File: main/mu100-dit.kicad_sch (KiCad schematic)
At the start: 14 parts, among them J1 Conn_01x10_Female, U1 TOTX-177L, U2 AK4103A

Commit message: Add reset circuit, remove need for reset
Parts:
- added C3: 0.1u/35V, Capacitor_SMD:C_0805_2012Metric_Pad1.18x1.45mm_HandSolder, symbol Device:C_Small
- added U3: APX809S-46SR-7, Package_TO_SOT_SMD:SOT-23_Handsoldering, symbol APX809S:APX809S-46SR-7
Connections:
- net +5V: now also C3.2, U3.3 (VCC)
- net GND: now also C3.1, U3.2 (GND)
- net RESET: now also U3.1 (*RESET); no longer J1.1 (Pin_1)
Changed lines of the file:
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@@
   (junction (at 115.57 130.81) (diameter 0) (color 0 0 0 0)
   )
+  (junction (at 97.79 108.585) (diameter 0) (color 0 0 0 0)
+  )
   (junction (at 53.34 81.28) (diameter 0) (color 0 0 0 0)
+  )
+  (junction (at 59.055 108.585) (diameter 0) (color 0 0 0 0)
   )
   (junction (at 58.42 83.185) (diameter 0) (color 0 0 0 0)
@@
     (stroke (width 0) (type solid) (color 0 0 0 0))
   )
+  (wire (pts (xy 97.79 104.14) (xy 97.79 108.585))
+    (stroke (width 0) (type default) (color 0 0 0 0))
+  )
   (wire (pts (xy 213.36 87.63) (xy 209.55 87.63))
     (stroke (width 0) (type default) (color 0 0 0 0))
@@
     (stroke (width 0) (type solid) (color 0 0 0 0))
   )
+  (wire (pts (xy 98.425 108.585) (xy 97.79 108.585))
+    (stroke (width 0) (type default) (color 0 0 0 0))
+  )
   (wire (pts (xy 168.91 100.33) (xy 213.36 100.33))
     (stroke (width 0) (type default) (color 0 0 0 0))
@@
     (stroke (width 0) (type solid) (color 0 0 0 0))
   )
+  (wire (pts (xy 59.055 108.585) (xy 82.55 108.585))
+    (stroke (width 0) (type default) (color 0 0 0 0))
+  )
   (wire (pts (xy 60.325 90.805) (xy 78.105 90.805))
     (stroke (width 0) (type default) (color 0 0 0 0))
   )
+  (wire (pts (xy 98.425 121.92) (xy 98.425 108.585))
+    (stroke (width 0) (type default) (color 0 0 0 0))
+  )
   (wire (pts (xy 168.91 125.73) (xy 179.07 125.73))
     (stroke (width 0) (type solid) (color 0 0 0 0))
@@
     (stroke (width 0) (type default) (color 0 0 0 0))
   )
+  (wire (pts (xy 57.785 108.585) (xy 59.055 108.585))
+    (stroke (width 0) (type default) (color 0 0 0 0))
+  )
   (wire (pts (xy 60.96 80.645) (xy 78.105 80.645))
     (stroke (width 0) (type default) (color 0 0 0 0))
@@
     (stroke (width 0) (type default) (color 0 0 0 0))
   )
+  (wire (pts (xy 57.785 121.92) (xy 57.785 108.585))
+    (stroke (width 0) (type default) (color 0 0 0 0))
+  )
   (wire (pts (xy 200.025 94.615) (xy 209.55 94.615))
     (stroke (width 0) (type default) (color 0 0 0 0))
@@
     (stroke (width 0) (type solid) (color 0 0 0 0))
   )
+  (wire (pts (xy 97.79 108.585) (xy 87.63 108.585))
+    (stroke (width 0) (type default) (color 0 0 0 0))
+  )
   (wire (pts (xy 53.34 81.28) (xy 58.42 81.28))
     (stroke (width 0) (type default) (color 0 0 0 0))
@@
     (stroke (width 0) (type solid) (color 0 0 0 0))
   )
+  (wire (pts (xy 101.6 124.46) (xy 98.425 124.46))
+    (stroke (width 0) (type default) (color 0 0 0 0))
+  )
   (wire (pts (xy 119.38 107.95) (xy 133.35 107.95))
     (stroke (width 0) (type solid) (color 0 0 0 0))
@@
   (label "RESET" (at 179.07 125.73 180)
     (effects (font (size 1.27 1.27)) (justify right bottom))
+  )
+  (label "RESET" (at 101.6 124.46 0)
+    (effects (font (size 1.27 1.27)) (justify left bottom))
   )
   (label "MCLK" (at 119.38 105.41 0)
@@
   )
   (label "LRCK" (at 61.595 95.885 0)
-    (effects (font (size 1.27 1.27)) (justify left bottom))
-  )
-  (label "RESET" (at 60.96 73.025 0)
     (effects (font (size 1.27 1.27)) (justify left bottom))
   )
@@
     (pin "1")
   )
+  (symbol (lib_id "Device:C_Small") (at 85.09 108.585 90) (mirror x) (unit 1)
+    (in_bom yes) (on_board yes)
+    (property "Reference" "C3" (id 0) (at 85.09 102.235 90))
+    (property "Value" "0.1u/35V" (id 1) (at 85.09 104.775 90))
+    (property "Footprint" "Capacitor_SMD:C_0805_2012Metric_Pad1.18x1.45mm_HandSolder" (id 2) (at 85.09 108.585 0)
+      (effects (font (size 1.27 1.27)) hide)
+    )
+    (property "Datasheet" "~" (id 3) (at 85.09 108.585 0)
+      (effects (font (size 1.27 1.27)) hide)
+    )
+    (pin "1")
+    (pin "2")
+  )
   (symbol (lib_id "power:+5V") (at 189.23 120.65 270) (mirror x) (unit 1)
     (in_bom yes) (on_board yes)
@@
   (symbol (lib_id "power:PWR_FLAG") (at 47.625 75.565 0) (unit 1)
     (in_bom yes) (on_board yes) (fields_autoplaced)
-    (property "Reference" "#FLG?" (id 0) (at 47.625 73.66 0)
+    (property "Reference" "#FLG0101" (id 0) (at 47.625 73.66 0)
       (effects (font (size 1.27 1.27)) hide)
     )
@@
     (pin "3")
   )
+  (symbol (lib_id "power:GND") (at 59.055 108.585 180) (unit 1)
+    (in_bom yes) (on_board yes)
+    (property "Reference" "#PWR01" (id 0) (at 59.055 102.235 0)
+      (effects (font (size 1.27 1.27)) hide)
+    )
+    (property "Value" "GND" (id 1) (at 58.9407 105.4099 90)
+      (effects (font (size 1.27 1.27)) (justify right))
+    )
+    (property "Footprint" "" (id 2) (at 59.055 108.585 0)
+      (effects (font (size 1.27 1.27)) hide)
+    )
+    (property "Datasheet" "" (id 3) (at 59.055 108.585 0)
+      (effects (font (size 1.27 1.27)) hide)
+    )
+    (pin "1")
+  )
   (symbol (lib_id "power:PWR_FLAG") (at 53.34 81.28 0) (unit 1)
     (in_bom yes) (on_board yes)
@@
     )
     (property "Datasheet" "" (id 3) (at 173.99 91.44 0)
+      (effects (font (size 1.27 1.27)) hide)
+    )
+    (pin "1")
+  )
+  (symbol (lib_id "power:+5V") (at 97.79 104.14 0) (unit 1)
+    (in_bom yes) (on_board yes)
+    (property "Reference" "#PWR02" (id 0) (at 97.79 107.95 0)
+      (effects (font (size 1.27 1.27)) hide)
+    )
+    (property "Value" "+5V" (id 1) (at 98.1583 99.8156 0))
+    (property "Footprint" "" (id 2) (at 97.79 104.14 0)
+      (effects (font (size 1.27 1.27)) hide)
+    )
+    (property "Datasheet" "" (id 3) (at 97.79 104.14 0)
       (effects (font (size 1.27 1.27)) hide)
     )
@@
     (pin "2")
   )
+  (symbol (lib_id "APX809S:APX809S-46SR-7") (at 57.785 121.92 0) (unit 1)
+    (in_bom yes) (on_board yes) (fields_autoplaced)
+    (property "Reference" "U3" (id 0) (at 78.105 110.49 0)
+      (effects (font (size 1.524 1.524)))
+    )
+    (property "Value" "APX809S-46SR-7" (id 1) (at 78.105 114.3 0)
+      (effects (font (size 1.524 1.524)))
+    )
+    (property "Footprint" "Package_TO_SOT_SMD:SOT-23_Handsoldering" (id 2) (at 78.105 115.824 0)
+      (effects (font (size 1.524 1.524)) hide)
+    )
+    (property "Datasheet" "" (id 3) (at 57.785 121.92 0)
+      (effects (font (size 1.524 1.524)))
+    )
+    (pin "1")
+    (pin "2")
+    (pin "3")
+  )
   (symbol (lib_id "Device:Jumper_NO_Small") (at 127 95.25 0) (unit 1)
     (in_bom yes) (on_board yes)
@@
   (symbol (lib_id "power:+5V") (at 39.37 75.565 0) (unit 1)
     (in_bom yes) (on_board yes) (fields_autoplaced)
-    (property "Reference" "#PWR?" (id 0) (at 39.37 79.375 0)
+    (property "Reference" "#PWR0103" (id 0) (at 39.37 79.375 0)
       (effects (font (size 1.27 1.27)) hide)
     )
@@
   )
   (symbol_instances
+    (path "/6b1a2a7c-5cca-46a5-9f28-c7f3c1b24f9a"
+      (reference "#FLG0101") (unit 1) (value "PWR_FLAG") (footprint "")
+    )
     (path "/8d936772-f6fa-4d42-bb01-ee988a455edf"
       (reference "#FLG0102") (unit 1) (value "PWR_FLAG") (footprint "")
     )
-    (path "/6b1a2a7c-5cca-46a5-9f28-c7f3c1b24f9a"
-      (reference "#FLG?") (unit 1) (value "PWR_FLAG") (footprint "")
+    (path "/87f96aed-c2f4-45df-be31-e068cb5e4f1c"
+      (reference "#PWR01") (unit 1) (value "GND") (footprint "")
+    )
+    (path "/9483f277-ba4b-4a90-8a24-6a8af6b58318"
+      (reference "#PWR02") (unit 1) (value "+5V") (footprint "")
     )
     (path "/6fa05153-0167-4b10-b6fb-ac9032665420"
@@
       (reference "#PWR0102") (unit 1) (value "GND") (footprint "")
     )
+    (path "/fc892e26-c3db-40cc-a8e8-335d5f7f739b"
+      (reference "#PWR0103") (unit 1) (value "+5V") (footprint "")
+    )
     (path "/8e1bf491-3d27-4187-838c-198fb49bfc42"
       (reference "#PWR0104") (unit 1) (value "+5V") (footprint "")
@@
       (reference "#PWR0116") (unit 1) (value "GND") (footprint "")
     )
-    (path "/fc892e26-c3db-40cc-a8e8-335d5f7f739b"
-      (reference "#PWR?") (unit 1) (value "+5V") (footprint "")
-    )
     (path "/10cc2e51-50b0-4331-8e90-6b91463bc461"
       (reference "C1") (unit 1) (value "0.1u/35V") (footprint "Capacitor_SMD:C_0805_2012Metric_Pad1.18x1.45mm_HandSolder")
@@
       (reference "C2") (unit 1) (value "0.1u/35V") (footprint "Capacitor_SMD:C_0805_2012Metric_Pad1.18x1.45mm_HandSolder")
     )
+    (path "/6163b631-b159-47b8-b51e-80be2eb24c7b"
+      (reference "C3") (unit 1) (value "0.1u/35V") (footprint "Capacitor_SMD:C_0805_2012Metric_Pad1.18x1.45mm_HandSolder")
+    )
     (path "/01106a52-6b7d-40fd-b165-c927be1f6a1d"
       (reference "J1") (unit 1) (value "Conn_01x10_Female") (footprint "Connector_JST:JST_PH_B10B-PH-K_1x10_P2.00mm_Vertical")
@@
       (reference "U2") (unit 1) (value "AK4103A") (footprint "Package_SO:TSSOP-24_6.1x7.8mm_P0.65mm")
     )
-  )
+    (path "/dc8fe5a7-ccb3-45b5-a637-48af9f79d36d"
+      (reference "U3") (unit 1) (value "APX809S-46SR-7") (footprint "Package_TO_SOT_SMD:SOT-23_Handsoldering")
+    )
+  )

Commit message: Move reset circuit to other side of board
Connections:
- no-connect marks 4 -> 5
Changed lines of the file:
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@@
   )
   (no_connect (at 133.35 120.65))
+  (no_connect (at 78.105 73.025))
   (no_connect (at 168.91 113.03))
   (no_connect (at 168.91 130.81))
@@
     (stroke (width 0) (type solid) (color 0 0 0 0))
   )
-  (wire (pts (xy 60.96 73.025) (xy 78.105 73.025))
-    (stroke (width 0) (type default) (color 0 0 0 0))
-  )
   (wire (pts (xy 115.57 128.27) (xy 119.38 128.27))

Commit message: Add header for optional coax output
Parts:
- added C4: 0.1u/35V, Capacitor_SMD:C_0805_2012Metric_Pad1.18x1.45mm_HandSolder, symbol Device:C_Small
- added H1, H2: MountingHole_Pad, MountingHole:MountingHole_3.2mm_M3_ISO7380_Pad_TopBottom, symbol Mechanical:MountingHole_Pad
- added J2: Conn_01x02_Male, Connector_PinHeader_2.54mm:PinHeader_1x02_P2.54mm_Vertical, symbol Connector:Conn_01x02_Male
- added R1: 330, Resistor_SMD:R_0805_2012Metric_Pad1.20x1.40mm_HandSolder, symbol Device:R_Small_US
- added R2: 100, Resistor_SMD:R_0805_2012Metric_Pad1.20x1.40mm_HandSolder, symbol Device:R_Small_US
- JP1, JP2, JP3, JP4, JP5, JP6, JP7, JP8, JP9: footprint Capacitor_SMD:C_0402_1005Metric_Pad0.74x0.62mm_HandSolder -> footprints:SolderJumper-Open_RoundedPad-custom
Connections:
- net GND: now also H1.1, H2.1, J2.2 (Pin_2), R2.1
- net TXP: now also R1.1
- new net: C4.1, R1.2, R2.2
- new net: C4.2, J2.1 (Pin_1)

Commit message: combine pcb projects
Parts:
- JP1, JP2, JP3, JP4, JP5, JP6, JP7, JP8, JP9: symbol Device:Jumper_NO_Small -> selfmade:Jumper_NO_Small
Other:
- added sheet MU100-dit-connector-board (MU100-dit-connector-board.kicad_sch)

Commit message: WIP
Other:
- removed sheet MU100-dit-connector-board
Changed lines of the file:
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@@
     (pin "1")
-  )
-  (sheet (at 156.21 17.145) (size 123.19 62.23) (fields_autoplaced)
-    (stroke (width 0.1524) (type solid) (color 0 0 0 0))
-    (fill (color 0 0 0 0.0000))
-    (property "Sheet name" "MU100-dit-connector-board" (id 0) (at 156.21 16.4334 0)
-      (effects (font (size 1.27 1.27)) (justify left bottom))
-    )
-    (property "Sheet file" "MU100-dit-connector-board.kicad_sch" (id 1) (at 156.21 79.9596 0)
-      (effects (font (size 1.27 1.27)) (justify left top))
-    )
   )
   (sheet_instances
     (path "/" (page "1"))
-    (path "/3b6b0ef8-cb49-4806-a385-9d93130ffdc0" (page "2"))
   )
   (symbol_instances
-    (path "/3b6b0ef8-cb49-4806-a385-9d93130ffdc0/e4471cac-1f08-4eb3-856b-eb1fe77f6adc"
-      (reference "#FLG01") (unit 1) (value "PWR_FLAG") (footprint "")
-    )
-    (path "/3b6b0ef8-cb49-4806-a385-9d93130ffdc0/e7e10faf-54ab-46bd-a086-b88bca32ddb0"
-      (reference "#FLG02") (unit 1) (value "PWR_FLAG") (footprint "")
-    )
-    (path "/3b6b0ef8-cb49-4806-a385-9d93130ffdc0/a738a49a-858c-41ea-928b-45f08a366eff"
-      (reference "#FLG0101") (unit 1) (value "PWR_FLAG") (footprint "")
-    )
-    (path "/3b6b0ef8-cb49-4806-a385-9d93130ffdc0/5f64b15b-3025-4a88-a75e-835b9bcbfbb2"
-      (reference "#FLG0102") (unit 1) (value "PWR_FLAG") (footprint "")
-    )
     (path "/886e7aef-6936-4447-a910-7e19a5795661"
       (reference "#FLG0103") (unit 1) (value "PWR_FLAG") (footprint "")
@@
       (reference "#PWR03") (unit 1) (value "GND") (footprint "")
     )
-    (path "/3b6b0ef8-cb49-4806-a385-9d93130ffdc0/18d685cd-dbe0-43a0-95a9-c950c9289910"
-      (reference "#PWR04") (unit 1) (value "GNDA") (footprint "")
-    )
-    (path "/3b6b0ef8-cb49-4806-a385-9d93130ffdc0/38ca63f7-9e89-479b-92e4-69f642c0bbff"
-      (reference "#PWR05") (unit 1) (value "GND") (footprint "")
-    )
-    (path "/3b6b0ef8-cb49-4806-a385-9d93130ffdc0/e4bf0dba-c0ae-4510-ab52-5f49cc86f479"
-      (reference "#PWR06") (unit 1) (value "+9VA") (footprint "")
-    )
-    (path "/3b6b0ef8-cb49-4806-a385-9d93130ffdc0/fdfc3f0a-437f-4206-b6a3-f5ef59d15f6b"
-      (reference "#PWR07") (unit 1) (value "+5V") (footprint "")
-    )
-    (path "/3b6b0ef8-cb49-4806-a385-9d93130ffdc0/964742c0-ee94-4927-91df-9434b273df16"
-      (reference "#PWR08") (unit 1) (value "+5V") (footprint "")
-    )
     (path "/6fa05153-0167-4b10-b6fb-ac9032665420"
       (reference "#PWR09") (unit 1) (value "GND") (footprint "")
-    )
-    (path "/3b6b0ef8-cb49-4806-a385-9d93130ffdc0/b9ad88d6-3ed9-406b-a6f9-0fb8cd5b9198"
-      (reference "#PWR010") (unit 1) (value "GND") (footprint "")
     )
     (path "/c07ca70e-8d5c-43f5-a020-41f14672ad82"
@@
       (reference "C4") (unit 1) (value "0.1u/35V") (footprint "Capacitor_SMD:C_0805_2012Metric_Pad1.18x1.45mm_HandSolder")
     )
-    (path "/3b6b0ef8-cb49-4806-a385-9d93130ffdc0/a0139dbf-800f-4b31-affb-7aba7e231628"
-      (reference "C5") (unit 1) (value "0.1u/35V") (footprint "Capacitor_SMD:C_0805_2012Metric_Pad1.18x1.45mm_HandSolder")
-    )
     (path "/296f96cb-3a0e-4d9e-a759-384daaf57c05"
       (reference "H1") (unit 1) (value "MountingHole_Pad") (footprint "MountingHole:MountingHole_3.2mm_M3_ISO7380_Pad_TopBottom")
@@
     (path "/d965a224-4ea6-434d-b44b-70b71e782e7a"
       (reference "J2") (unit 1) (value "Conn_01x02_Male") (footprint "Connector_PinHeader_2.54mm:PinHeader_1x02_P2.54mm_Vertical")
-    )
-    (path "/3b6b0ef8-cb49-4806-a385-9d93130ffdc0/d8f1aa4a-2f21-4570-b6e4-a5df899c3581"
-      (reference "J3") (unit 1) (value "Conn_01x17_Male") (footprint "Connector_PinHeader_2.00mm:PinHeader_1x17_P2.00mm_Vertical")
-    )
-    (path "/3b6b0ef8-cb49-4806-a385-9d93130ffdc0/2cdad8ef-b5c8-42b4-91da-9d5f6d9b006b"
-      (reference "J4") (unit 1) (value "51247 Molex") (footprint "Molex-52147-1710:Molex_Wire-Trap_52147-1710_1x17_P2.00mm_Vertical")
-    )
-    (path "/3b6b0ef8-cb49-4806-a385-9d93130ffdc0/038a3fe5-035a-4e1c-ba13-3474b63e4a27"
-      (reference "J5") (unit 1) (value "JST-PH_01x10_Socket") (footprint "Connector_JST:JST_PH_B10B-PH-K_1x10_P2.00mm_Vertical")
     )
     (path "/9645fdbc-abbb-4422-938b-7ae720c720cd"
@@
       (reference "R2") (unit 1) (value "100") (footprint "Resistor_SMD:R_0805_2012Metric_Pad1.20x1.40mm_HandSolder")
     )
-    (path "/3b6b0ef8-cb49-4806-a385-9d93130ffdc0/f888d71b-37ae-40d1-b9f5-0cb7096abe99"
-      (reference "R3") (unit 1) (value "47") (footprint "Resistor_SMD:R_0805_2012Metric_Pad1.20x1.40mm_HandSolder")
-    )
-    (path "/3b6b0ef8-cb49-4806-a385-9d93130ffdc0/e2ae356e-ef23-4b31-8a5e-0f3c3f7013b8"
-      (reference "R4") (unit 1) (value "47") (footprint "Resistor_SMD:R_0805_2012Metric_Pad1.20x1.40mm_HandSolder")
-    )
-    (path "/3b6b0ef8-cb49-4806-a385-9d93130ffdc0/c1bdbf84-278b-4573-9ff7-b7c67a0b3822"
-      (reference "R5") (unit 1) (value "47") (footprint "Resistor_SMD:R_0805_2012Metric_Pad1.20x1.40mm_HandSolder")
-    )
-    (path "/3b6b0ef8-cb49-4806-a385-9d93130ffdc0/68f4e72b-a890-47b0-8f3f-e8d32a954350"
-      (reference "R6") (unit 1) (value "47") (footprint "Resistor_SMD:R_0805_2012Metric_Pad1.20x1.40mm_HandSolder")
-    )
     (path "/827e08b4-e65f-4e14-95ac-524ec991f7af"

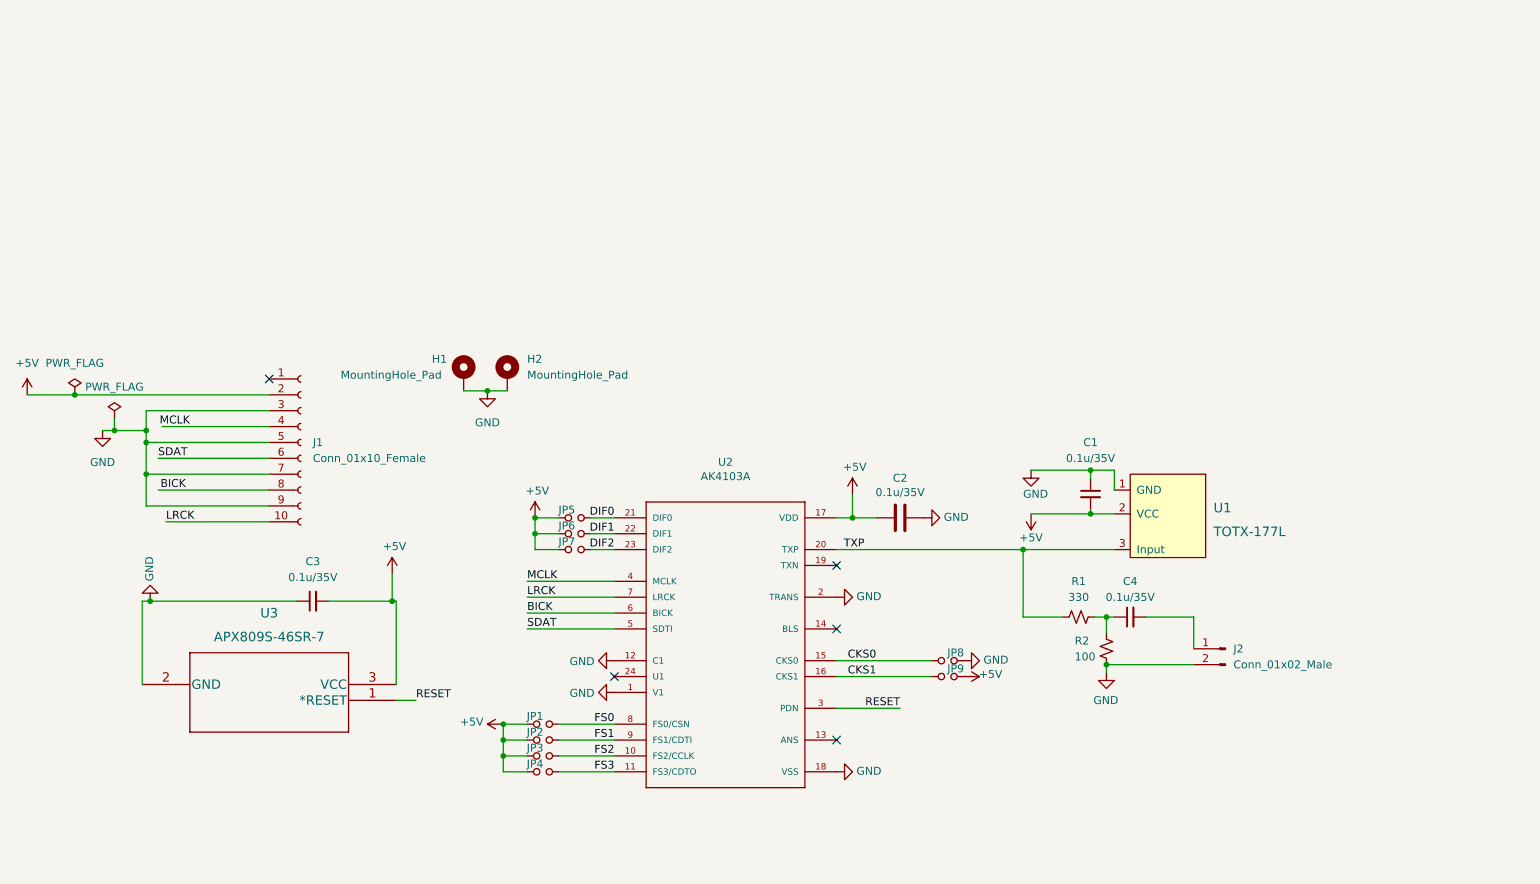
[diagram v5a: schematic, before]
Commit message: Clean up schematics and board drawings
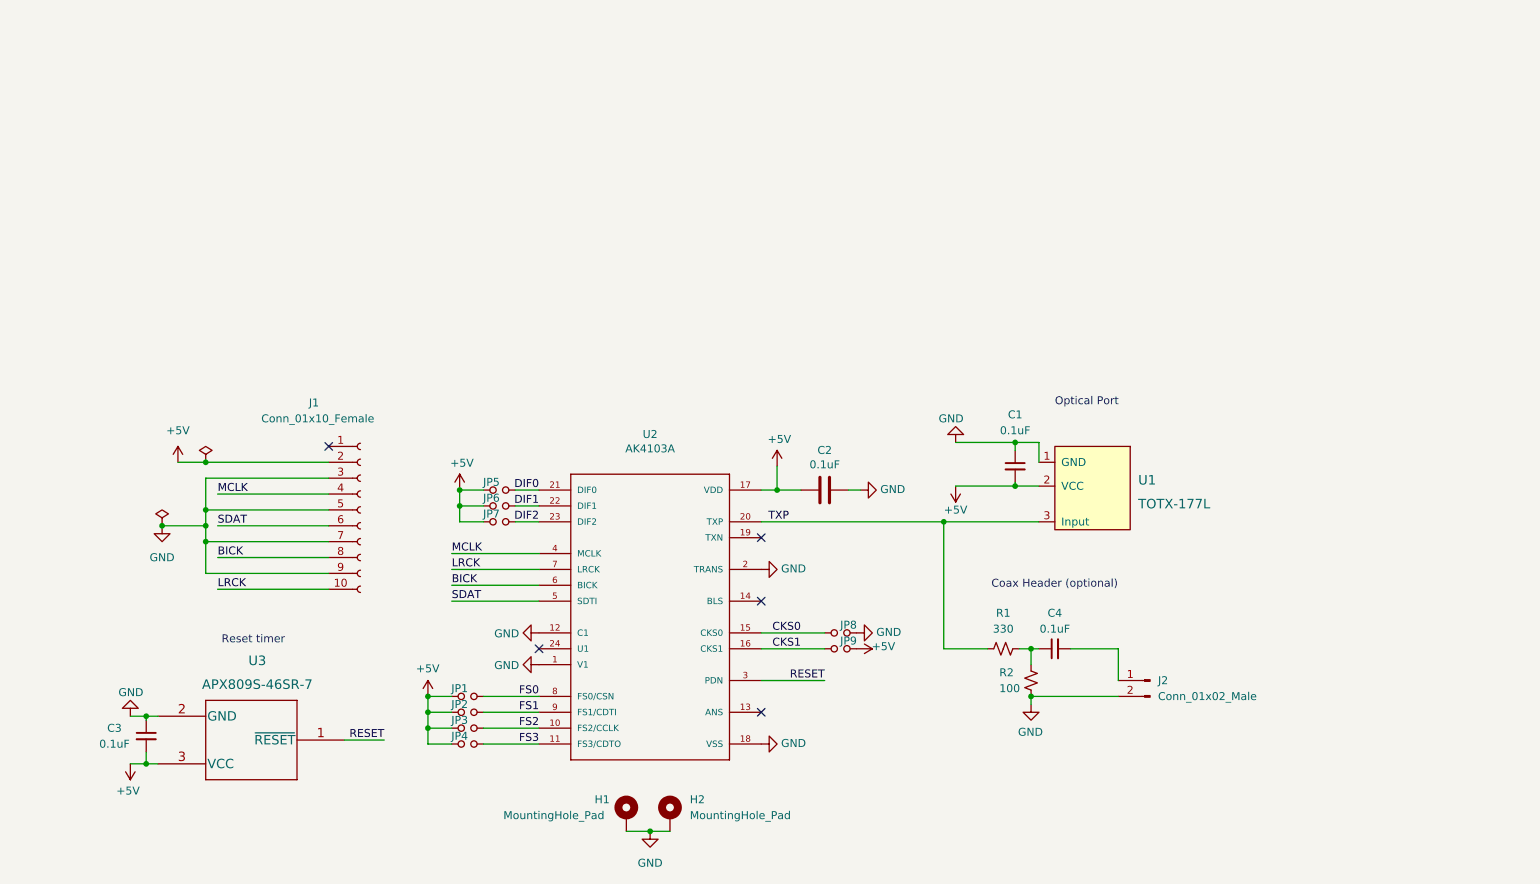
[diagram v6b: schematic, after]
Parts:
- C1, C2, C3, C4: value 0.1u/35V -> 0.1uF
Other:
- note added: "Coax Header (optional)"
- note added: "Optical Port"
- note added: "Reset timer"
- moved on the sheet: C1, C2, C4, H1, H2, J1, J2, JP1, JP2, JP3, JP4, JP5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
